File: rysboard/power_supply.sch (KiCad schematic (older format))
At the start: 36 parts, among them J19 Fan_Connector, Q1 DMP3036SSD-13, Q3 NST847BDP6T5G, Q4 DMP3036SSD-13, Q5 DMP3036SSD-13, U3 ST1S10, U6 L78L33_SO8

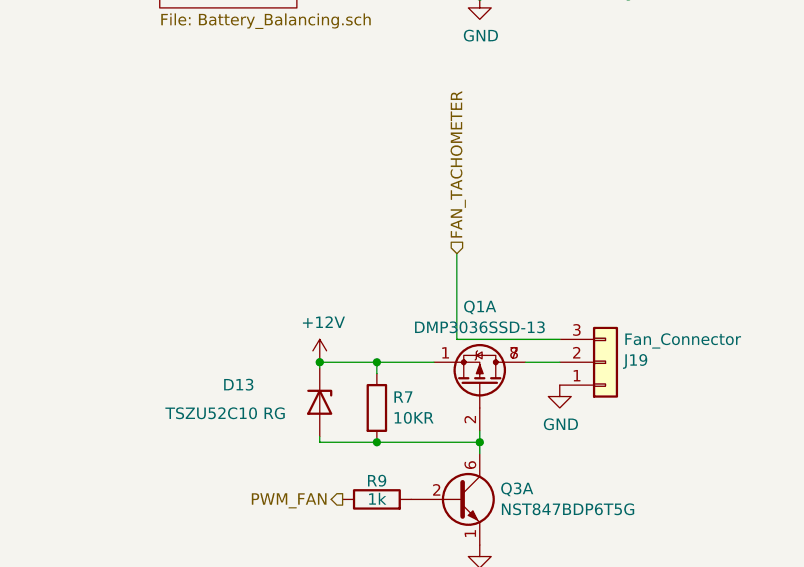
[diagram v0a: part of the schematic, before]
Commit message: ltc4007 configured
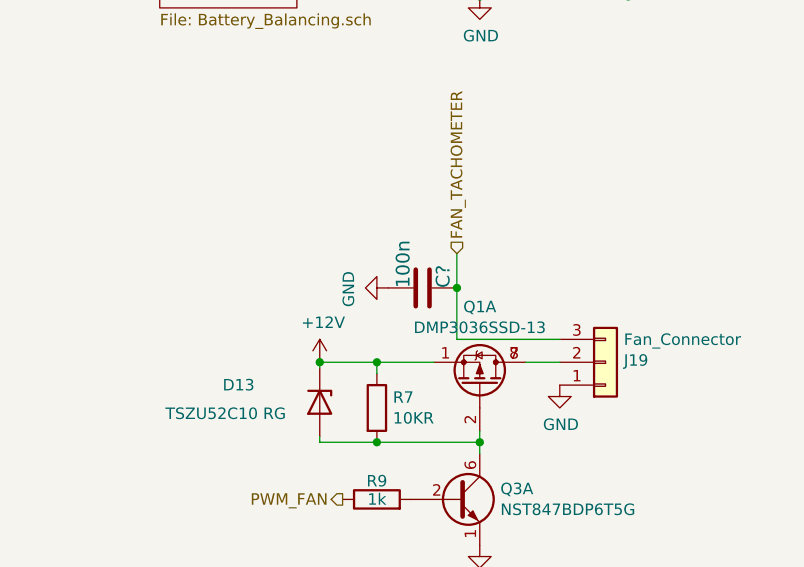
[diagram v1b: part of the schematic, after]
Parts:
- added C?: 100n, Capacitor_SMD:C_0603_1608Metric, symbol Device:C
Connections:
- net FAN_TACHOMETER: now also C?.1
- net GND: now also C?.2
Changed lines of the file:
@@
 FAN_TACHOMETER
 Wire Wire Line
-	2300 2975 2300 3350
+	2300 2975 2300 3125
 Wire Wire Line
 	2300 3350 2750 3350
@@
 $EndComp
 Connection ~ 5400 1350
+$Comp
+L Device:C C?
+U 1 1 604492BA
+P 2150 3125
+AR Path="/5EB7428E/604492BA" Ref="C?"  Part="1"
+AR Path="/5E8FCBC6/604492BA" Ref="C?"  Part="1"
+F 0 "C?" H 2150 3250 60  0000 R TNN
+F 1 "100n" H 2150 3075 60  0000 R TNN
+F 2 "Capacitor_SMD:C_0603_1608Metric" H 2050 3215 60  0001 C CNN
+F 3 "~" H 2050 3215 60  0001 C CNN
+	1    2150 3125
+	0    1    1    0
+$EndComp
+Connection ~ 2300 3125
+Wire Wire Line
+	2300 3125 2300 3350
+$Comp
+L power:GND #PWR?
+U 1 1 6044A19C
+P 2000 3125
+F 0 "#PWR?" H 2000 2875 50  0001 C CNN
+F 1 "GND" H 2005 2952 50  0000 C CNN
+F 2 "" H 2000 3125 50  0001 C CNN
+F 3 "" H 2000 3125 50  0001 C CNN
+	1    2000 3125
+	0    1    1    0
+$EndComp
 $EndSCHEMATC

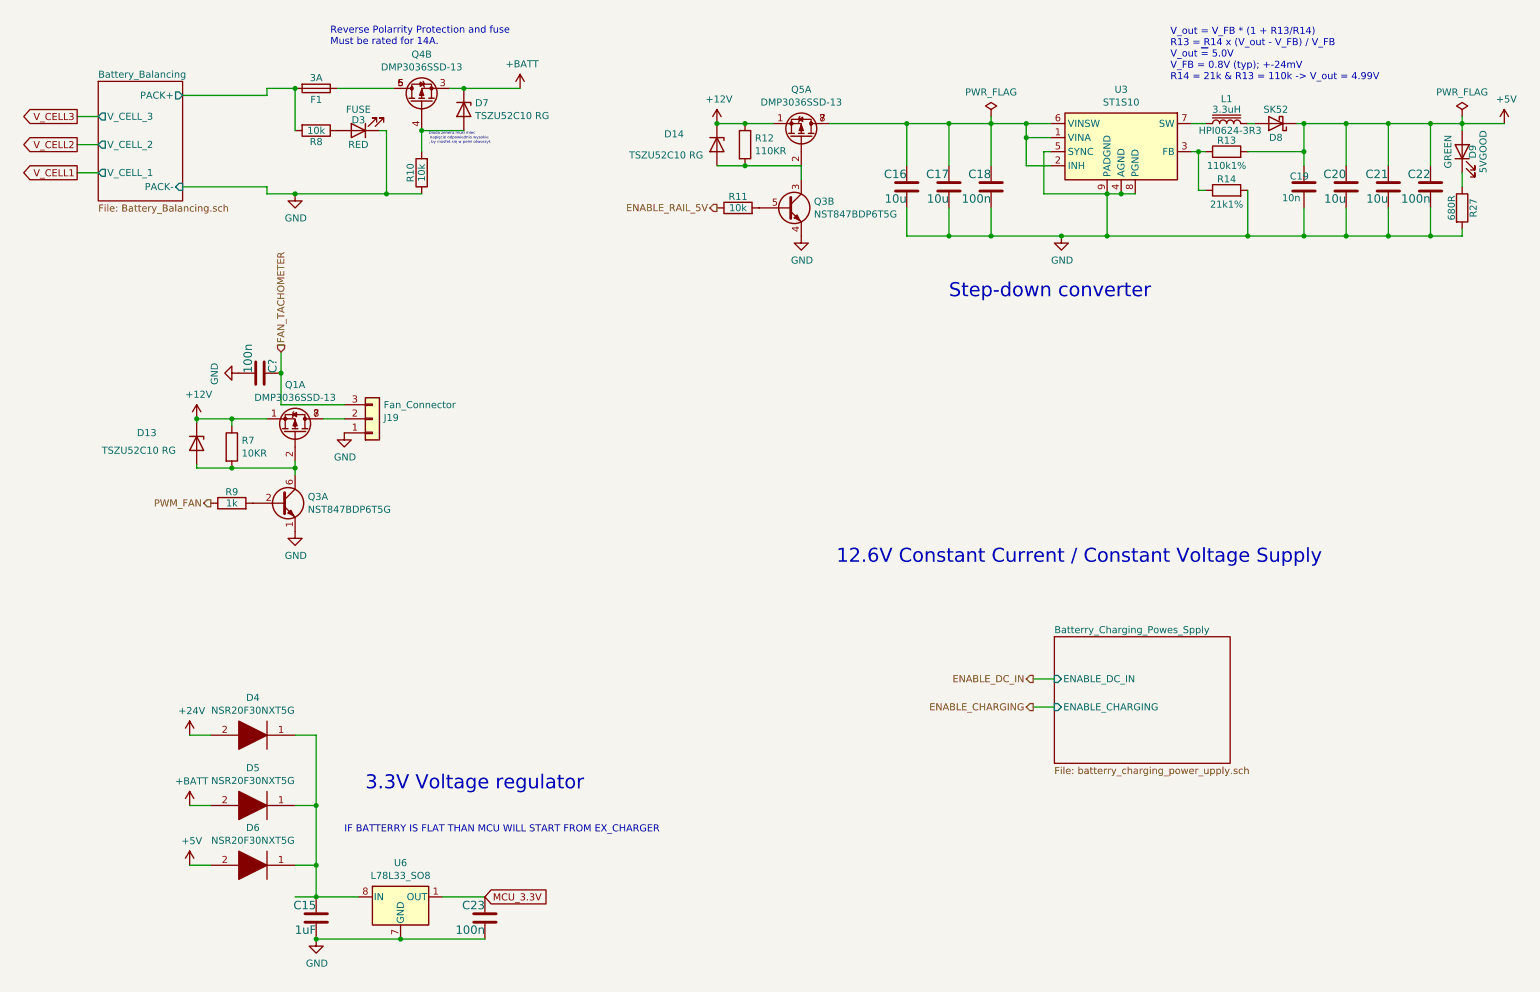
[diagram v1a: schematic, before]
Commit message: LTC4007 done
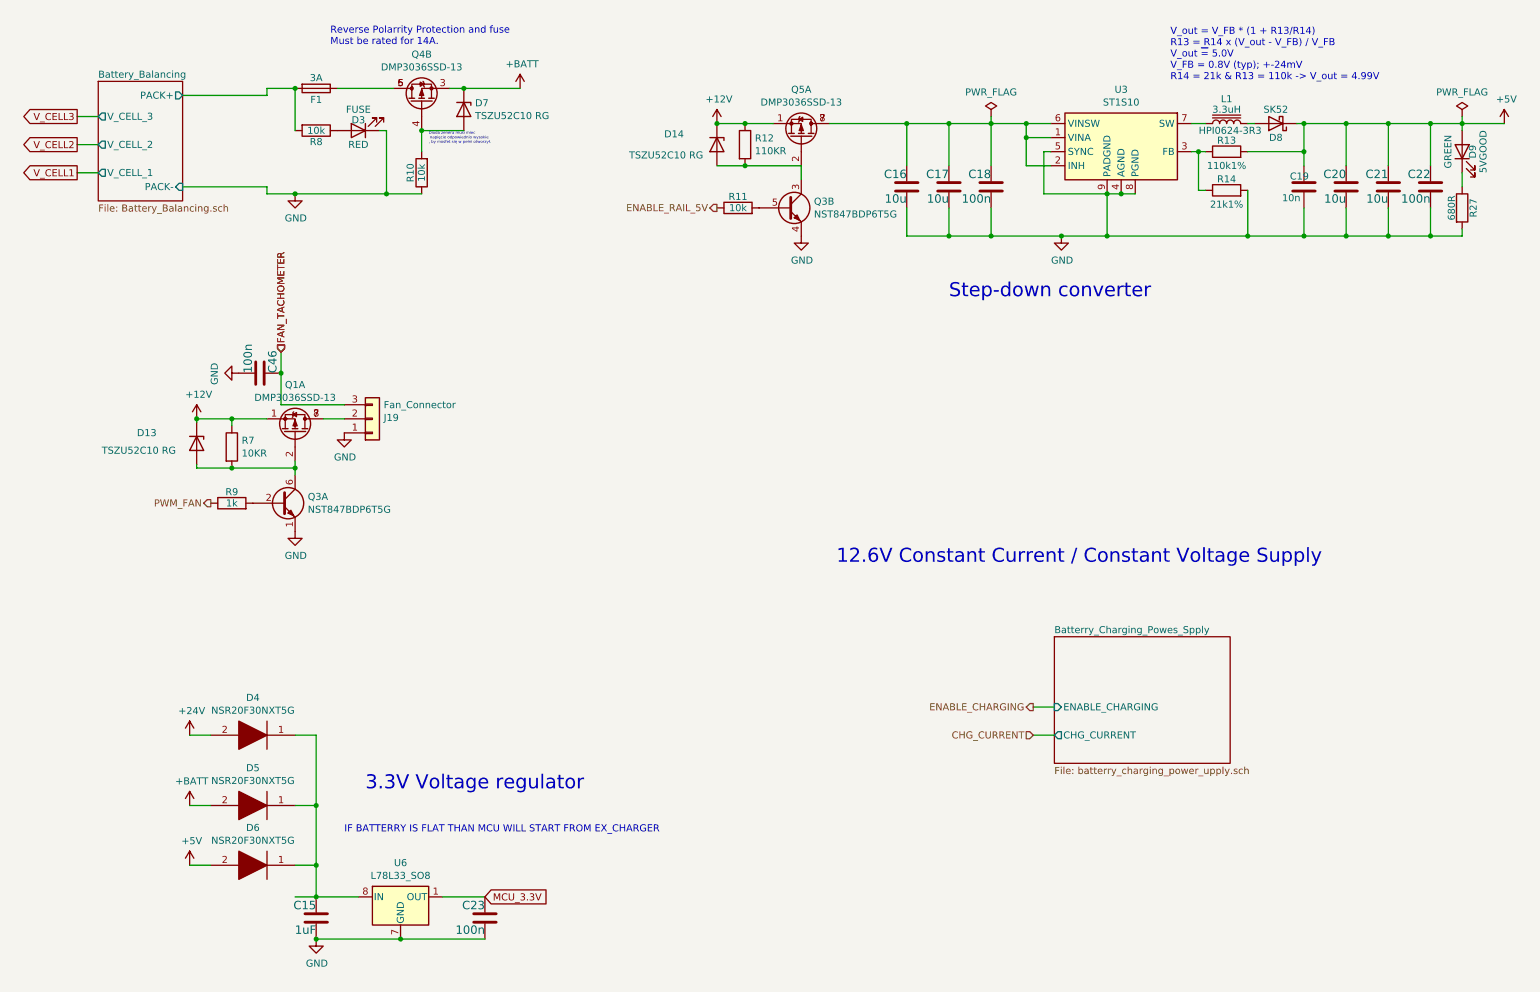
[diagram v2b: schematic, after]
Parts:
- J19: footprint (none) -> Connector_PinHeader_2.54mm:PinHeader_1x03_P2.54mm_Vertical
- gave numbers to parts that had none: 1
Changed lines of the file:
@@
 F0 "Batterry_Charging_Powes_Spply" 50
 F1 "batterry_charging_power_upply.sch" 50
-F2 "ENABLE_DC_IN" I L 7800 5300 50
-F3 "ENABLE_CHARGING" I L 7800 5500 50
+F2 "ENABLE_CHARGING" I L 7800 5500 50
+F3 "CHG_CURRENT" O L 7800 5700 50
 $EndSheet
 $Comp
@@
 F 0 "J19" H 3030 3442 50  0000 L CNN
 F 1 "Fan_Connector" H 3030 3351 50  0000 L CNN
-F 2 "" H 2950 3450 50  0001 C CNN
+F 2 "Connector_PinHeader_2.54mm:PinHeader_1x03_P2.54mm_Vertical" H 2950 3450 50  0001 C CNN
 F 3 "~" H 2950 3450 50  0001 C CNN
 	1    2950 3450
@@
 Text HLabel 1800 4050 0    50   Output ~ 0
 PWM_FAN
-Text HLabel 7650 5300 0    50   Output ~ 0
-ENABLE_DC_IN
-Wire Wire Line
-	7800 5300 7650 5300
 $Comp
 L rysboard:NST847BDP6T5G Q3
@@
 P 2150 3125
 AR Path="/5EB7428E/604492BA" Ref="C?"  Part="1"
-AR Path="/5E8FCBC6/604492BA" Ref="C?"  Part="1"
-F 0 "C?" H 2150 3250 60  0000 R TNN
+AR Path="/5E8FCBC6/604492BA" Ref="C46"  Part="1"
+F 0 "C46" H 2150 3250 60  0000 R TNN
 F 1 "100n" H 2150 3075 60  0000 R TNN
 F 2 "Capacitor_SMD:C_0603_1608Metric" H 2050 3215 60  0001 C CNN
@@
 	2300 3125 2300 3350
 $Comp
-L power:GND #PWR?
+L power:GND #PWR0111
 U 1 1 6044A19C
 P 2000 3125
-F 0 "#PWR?" H 2000 2875 50  0001 C CNN
+F 0 "#PWR0111" H 2000 2875 50  0001 C CNN
 F 1 "GND" H 2005 2952 50  0000 C CNN
 F 2 "" H 2000 3125 50  0001 C CNN
@@
 	0    1    1    0
 $EndComp
+Text HLabel 7650 5700 0    50   Input ~ 0
+CHG_CURRENT
+Wire Wire Line
+	7650 5700 7800 5700
+Text HLabel 2300 2975 1    50   Input ~ 0
+FAN_TACHOMETER
 $EndSCHEMATC

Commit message: More Work. RPI can now programm STM32 via GPIO
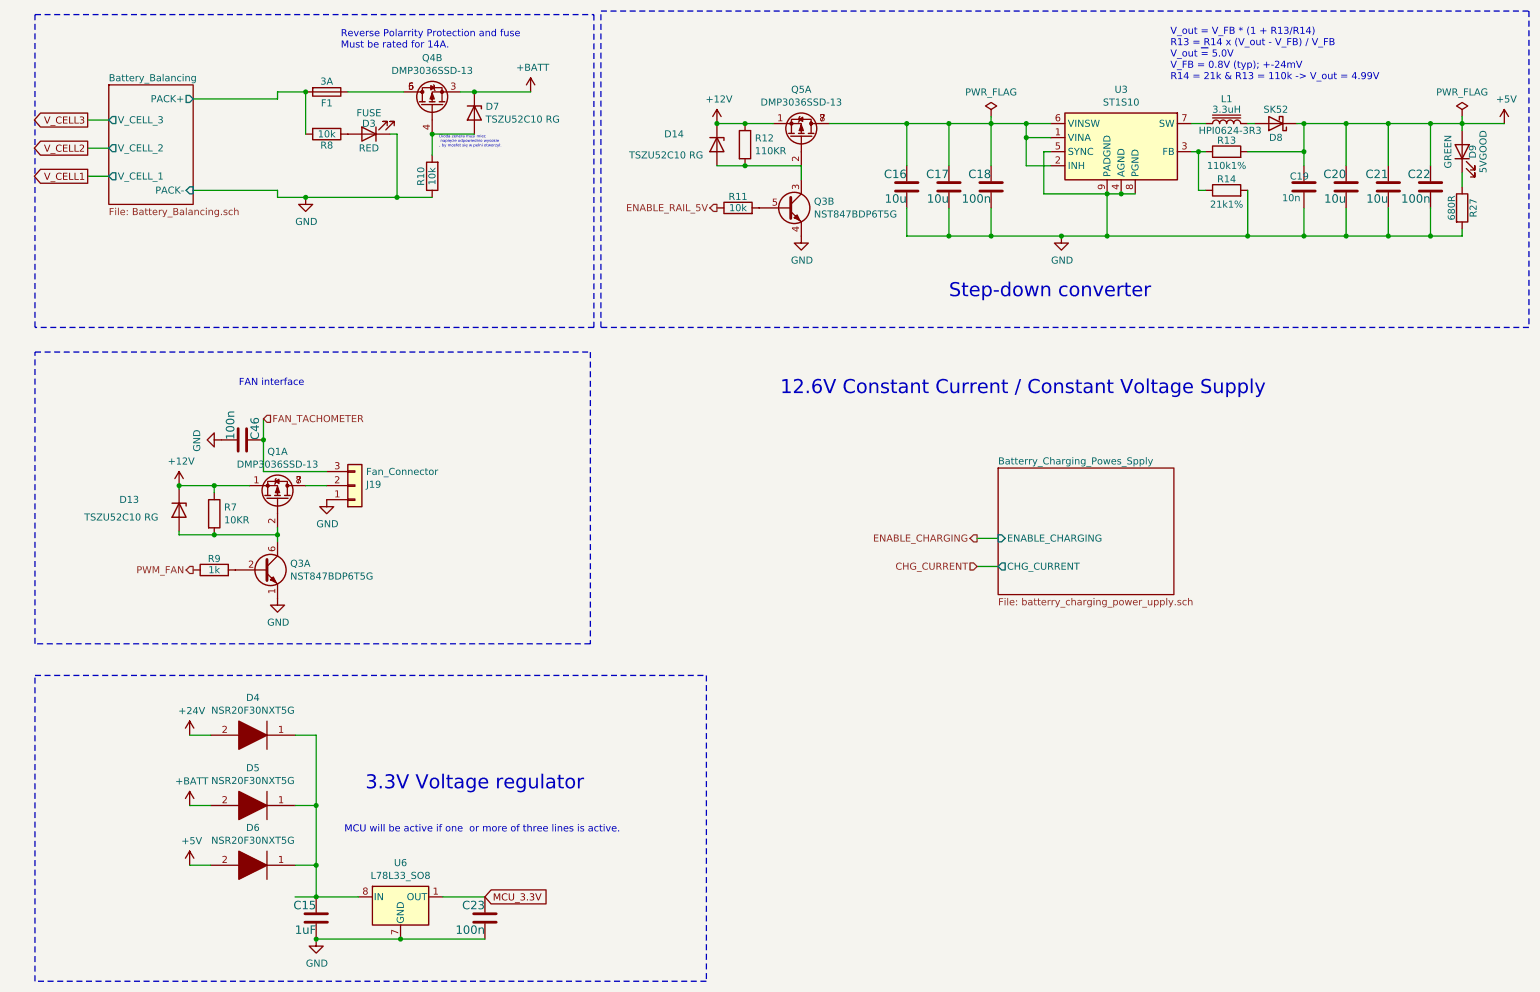
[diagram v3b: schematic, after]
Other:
- note added: "FAN interface"
- note added: "MCU will be active if one or more of three lines is active.\n"
- note removed: "IF BATTERRY IS FLAT THAN MCU WILL START FROM EX_CHARGER\n"
- moved on the sheet: C46, D13, D3, D7, F1, J19, Q1A, Q3A, Q4B, R10, R7, R8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

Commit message: cleanup and energy managment scheeme started
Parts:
- removed D3: RED, LED_SMD:LED_0805_2012Metric, symbol Device:LED
- removed D7: TSZU52C10 RG, Diode_SMD:D_0603_1608Metric, symbol Device:D_Zener
- removed F1: 3A, Fuse:Fuse_1206_3216Metric, symbol Device:Fuse
- removed Q4: DMP3036SSD-13, Package_SO:SO-8_3.9x4.9mm_P1.27mm, symbol rysboard:DMP3036SSD-13
- removed R10, R8: 10k, Resistor_SMD:R_0603_1608Metric, symbol Device:R
- added D?: TSZU52C10 RG, Diode_SMD:D_0603_1608Metric, symbol Device:D_Zener
- added Q?: DMP3036SSD-13, Package_SO:SO-8_3.9x4.9mm_P1.27mm, symbol rysboard:DMP3036SSD-13
- added Q?: NST847BDP6T5G, Package_TO_SOT_SMD:SOT-963, symbol rysboard:NST847BDP6T5G
- added R?: 110KR, Resistor_SMD:R_0603_1608Metric, symbol Device:R
- added R?: 10k, Resistor_SMD:R_0603_1608Metric, symbol Device:R
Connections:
- net +12V: now also Q?.7 (d), Q?.8 (d)
- net +BATT: now also D?.1 (K), Q?.1 (S1), R?.1
- new net: Q?.2 (G1), Q?.3 (C2), R?.2
- new net: Q?.5 (B2), R?.2
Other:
- note removed: "Dioda zenera musi miec\n napięcie odpowiednio wysokie\n, by mosfet się w pełni otworzył."
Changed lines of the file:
@@
 Step-down converter
-$Comp
-L Device:Fuse F1
-U 1 1 5EC1A2C9
-P 2625 1125
-F 0 "F1" V 2705 1125 50  0000 C CNN
-F 1 "3A" V 2550 1125 50  0000 C CNN
-F 2 "Fuse:Fuse_1206_3216Metric" V 2555 1125 50  0001 C CNN
-F 3 "~" H 2625 1125 50  0001 C CNN
-	1    2625 1125
-	0    1    1    0
-$EndComp
-Wire Wire Line
-	2475 1125 2475 1425
-Wire Wire Line
-	3075 1425 3125 1425
 $Comp
 L power:GND #PWR018
 U 1 1 5E91776C
-P 2475 1875
-F 0 "#PWR018" H 2475 1625 50  0001 C CNN
-F 1 "GND" H 2480 1702 50  0000 C CNN
-F 2 "" H 2475 1875 50  0001 C CNN
-F 3 "" H 2475 1875 50  0001 C CNN
-	1    2475 1875
-	1    0    0    -1
-$EndComp
-$Comp
-L Device:R R8
-U 1 1 5EC1A2DB
-P 2625 1425
-F 0 "R8" V 2705 1425 50  0000 C CNN
-F 1 "10k" V 2625 1425 50  0000 C CNN
-F 2 "Resistor_SMD:R_0603_1608Metric" V 2555 1425 50  0001 C CNN
-F 3 "~" H 2625 1425 50  0001 C CNN
-	1    2625 1425
-	0    1    1    0
-$EndComp
-$Comp
-L Device:LED D3
-U 1 1 5EC1A2E1
-P 2925 1425
-F 0 "D3" H 2925 1350 50  0000 C CNN
-F 1 "RED" H 2925 1525 50  0000 C CNN
-F 2 "LED_SMD:LED_0805_2012Metric" H 2925 1425 50  0001 C CNN
-F 3 "~" H 2925 1425 50  0001 C CNN
-F 4 "FUSE" H 2925 1275 50  0000 C CNN "Comment"
-	1    2925 1425
-	-1   0    0    1
+P 2175 1825
+F 0 "#PWR018" H 2175 1575 50  0001 C CNN
+F 1 "GND" H 2180 1652 50  0000 C CNN
+F 2 "" H 2175 1825 50  0001 C CNN
+F 3 "" H 2175 1825 50  0001 C CNN
+	1    2175 1825
+	1    0    0    -1
 $EndComp
 Wire Wire Line
 	2400 6850 2550 6850
 Connection ~ 2550 6850
-$Comp
-L Device:R R10
-U 1 1 5FECF6D8
-P 3375 1725
-F 0 "R10" V 3455 1725 50  0000 C CNN
-F 1 "10k" V 3375 1725 50  0000 C CNN
-F 2 "Resistor_SMD:R_0603_1608Metric" V 3305 1725 50  0001 C CNN
-F 3 "~" H 3375 1725 50  0001 C CNN
-	1    3375 1725
-	-1   0    0    1
-$EndComp
-Wire Wire Line
-	3375 1425 3375 1575
-$Comp
-L Device:D_Zener D7
-U 1 1 5FED8493
-P 3675 1275
-F 0 "D7" V 3629 1355 50  0000 L CNN
-F 1 "TSZU52C10 RG" V 3720 1355 50  0000 L CNN
-F 2 "Diode_SMD:D_0603_1608Metric" H 3675 1275 50  0001 C CNN
-F 3 "~" H 3675 1275 50  0001 C CNN
-	1    3675 1275
-	0    1    1    0
-$EndComp
-Wire Wire Line
-	3575 1125 3675 1125
-Wire Wire Line
-	3675 1425 3375 1425
-Wire Wire Line
-	4075 1125 3675 1125
-Connection ~ 3675 1125
-Text Notes 3425 1525 0    20   ~ 0
-Dioda zenera musi miec\n napięcie odpowiednio wysokie\n, by mosfet się w pełni otworzył.
 Text Notes 2725 825  0    50   ~ 0
 Reverse Polarrity Protection and fuse\nMust be rated for 14A.\n
@@
 MCU_3.3V
 Wire Wire Line
-	1675 1175 2275 1175
-Wire Wire Line
-	2275 1175 2275 1125
-Wire Wire Line
-	2275 1125 2475 1125
-Connection ~ 2475 1125
-Wire Wire Line
-	2475 1875 3125 1875
-Connection ~ 2475 1875
-Wire Wire Line
-	2475 1875 2275 1875
-Wire Wire Line
-	2275 1875 2275 1825
-Wire Wire Line
-	2275 1825 1675 1825
-Wire Wire Line
-	3125 1425 3125 1875
-Connection ~ 3125 1875
-Wire Wire Line
-	3125 1875 3375 1875
+	1675 1175 2150 1175
 $Sheet
 S 7400 3800 1250 900
@@
 L power:+BATT #PWR034
 U 1 1 605BC324
-P 4075 1125
-F 0 "#PWR034" H 4075 975 50  0001 C CNN
-F 1 "+BATT" H 4090 1298 50  0000 C CNN
-F 2 "" H 4075 1125 50  0001 C CNN
-F 3 "" H 4075 1125 50  0001 C CNN
-	1    4075 1125
+P 2150 1175
+F 0 "#PWR034" H 2150 1025 50  0001 C CNN
+F 1 "+BATT" H 2165 1348 50  0000 C CNN
+F 2 "" H 2150 1175 50  0001 C CNN
+F 3 "" H 2150 1175 50  0001 C CNN
+	1    2150 1175
 	1    0    0    -1
 $EndComp
@@
 V_CELL1
 Wire Wire Line
-	2775 1125 3175 1125
-Wire Wire Line
 	5600 1650 6000 1650
-$Comp
-L rysboard:DMP3036SSD-13 Q4
-U 2 1 6051D51B
-P 3375 1225
-F 0 "Q4" V 3717 1225 50  0000 C CNN
-F 1 "DMP3036SSD-13" V 3626 1225 50  0000 C CNN
-F 2 "Package_SO:SO-8_3.9x4.9mm_P1.27mm" H 3575 1150 50  0001 L CIN
-F 3 "" H 3375 1225 50  0001 L CNN
-	2    3375 1225
-	0    -1   -1   0
-$EndComp
-Connection ~ 3375 1425
 $Comp
 L rysboard:DMP3036SSD-13 Q5
@@
 Wire Notes Line
 	550  7450 550  5275
+Wire Wire Line
+	2175 1825 1675 1825
+$Comp
+L rysboard:DMP3036SSD-13 Q?
+U 1 1 60615F71
+P 3650 1275
+F 0 "Q?" V 3992 1275 50  0000 C CNN
+F 1 "DMP3036SSD-13" V 3901 1275 50  0000 C CNN
+F 2 "Package_SO:SO-8_3.9x4.9mm_P1.27mm" H 3850 1200 50  0001 L CIN
+F 3 "" H 3650 1275 50  0001 L CNN
+	1    3650 1275
+	0    1    -1   0
+$EndComp
+$Comp
+L Device:D_Zener D?
+U 1 1 60616F79
+P 2925 1325
+F 0 "D?" V 2850 950 50  0000 L CNN
+F 1 "TSZU52C10 RG" V 3000 700 50  0000 L CNN
+F 2 "Diode_SMD:D_0603_1608Metric" H 2925 1325 50  0001 C CNN
+F 3 "~" H 2925 1325 50  0001 C CNN
+	1    2925 1325
+	0    1    1    0
+$EndComp
+$Comp
+L Device:R R?
+U 1 1 606173BC
+P 3225 1325
+F 0 "R?" H 3295 1371 50  0000 L CNN
+F 1 "110KR" H 3295 1280 50  0000 L CNN
+F 2 "Resistor_SMD:R_0603_1608Metric" V 3155 1325 50  0001 C CNN
+F 3 "~" H 3225 1325 50  0001 C CNN
+	1    3225 1325
+	1    0    0    -1
+$EndComp
+$Comp
+L rysboard:NST847BDP6T5G Q?
+U 2 1 6061762B
+P 3550 1875
+F 0 "Q?" H 3740 1921 50  0000 L CNN
+F 1 "NST847BDP6T5G" H 3740 1830 50  0000 L CNN
+F 2 "Package_TO_SOT_SMD:SOT-963" H 3750 1975 50  0001 C CNN
+F 3 "~" H 3550 1875 50  0001 C CNN
+	2    3550 1875
+	1    0    0    -1
+$EndComp
+$Comp
+L Device:R R?
+U 1 1 60617A11
+P 3200 1875
+F 0 "R?" V 3280 1875 50  0000 C CNN
+F 1 "10k" V 3200 1875 50  0000 C CNN
+F 2 "Resistor_SMD:R_0603_1608Metric" V 3130 1875 50  0001 C CNN
+F 3 "~" H 3200 1875 50  0001 C CNN
+	1    3200 1875
+	0    -1   -1   0
+$EndComp
+$Comp
+L power:+BATT #PWR?
+U 1 1 60617D1F
+P 2925 1175
+F 0 "#PWR?" H 2925 1025 50  0001 C CNN
+F 1 "+BATT" H 2940 1348 50  0000 C CNN
+F 2 "" H 2925 1175 50  0001 C CNN
+F 3 "" H 2925 1175 50  0001 C CNN
+	1    2925 1175
+	1    0    0    -1
+$EndComp
+Wire Wire Line
+	2925 1175 3225 1175
+Connection ~ 2925 1175
+Connection ~ 3225 1175
+Wire Wire Line
+	3225 1175 3450 1175
+Wire Wire Line
+	3225 1475 3650 1475
+Wire Wire Line
+	2950 1475 3225 1475
+Connection ~ 3225 1475
+Wire Wire Line
+	3650 1475 3650 1675
+Connection ~ 3650 1475
+$Comp
+L power:GND #PWR?
+U 1 1 606277F2
+P 3625 2050
+F 0 "#PWR?" H 3625 1800 50  0001 C CNN
+F 1 "GND" H 3630 1877 50  0000 C CNN
+F 2 "" H 3625 2050 50  0001 C CNN
+F 3 "" H 3625 2050 50  0001 C CNN
+	1    3625 2050
+	1    0    0    -1
+$EndComp
+$Comp
+L power:+12V #PWR?
+U 1 1 60627A51
+P 4125 1175
+F 0 "#PWR?" H 4125 1025 50  0001 C CNN
+F 1 "+12V" H 4140 1348 50  0000 C CNN
+F 2 "" H 4125 1175 50  0001 C CNN
+F 3 "" H 4125 1175 50  0001 C CNN
+	1    4125 1175
+	1    0    0    -1
+$EndComp
+Wire Wire Line
+	4125 1175 3850 1175
 $EndSCHEMATC
